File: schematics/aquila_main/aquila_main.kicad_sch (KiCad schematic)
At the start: 95 parts, among them IC1 TPS62152, IC2 TPS62132

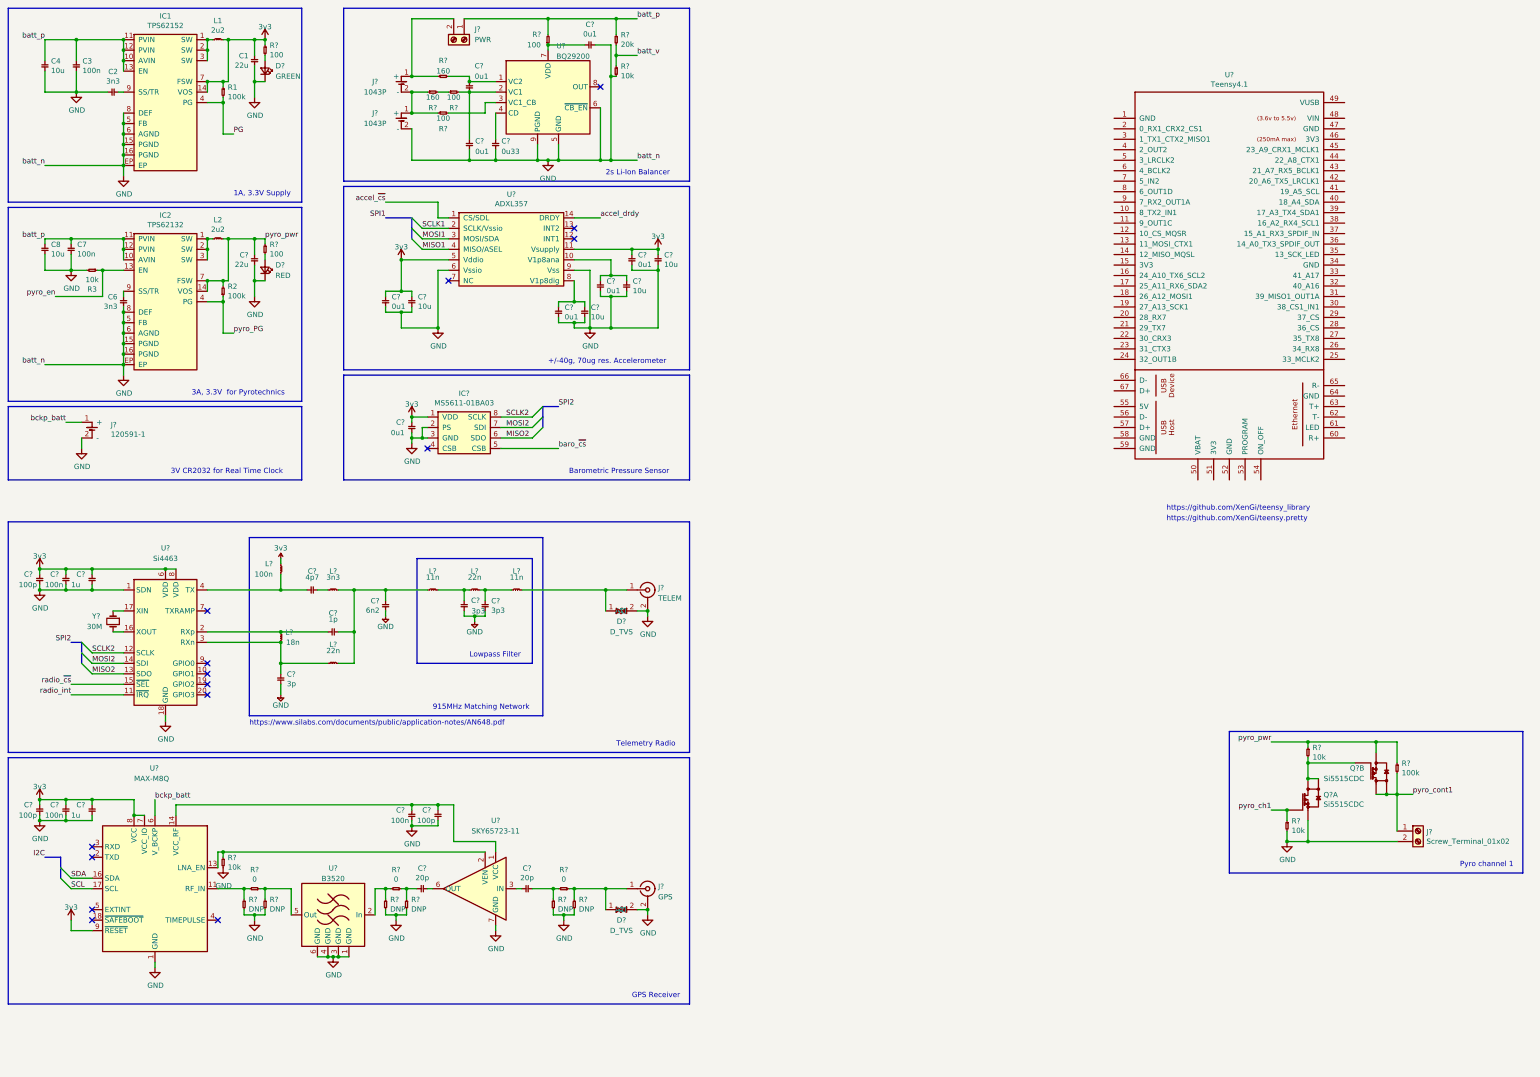
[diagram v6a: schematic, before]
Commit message: added connections for Teensy uC
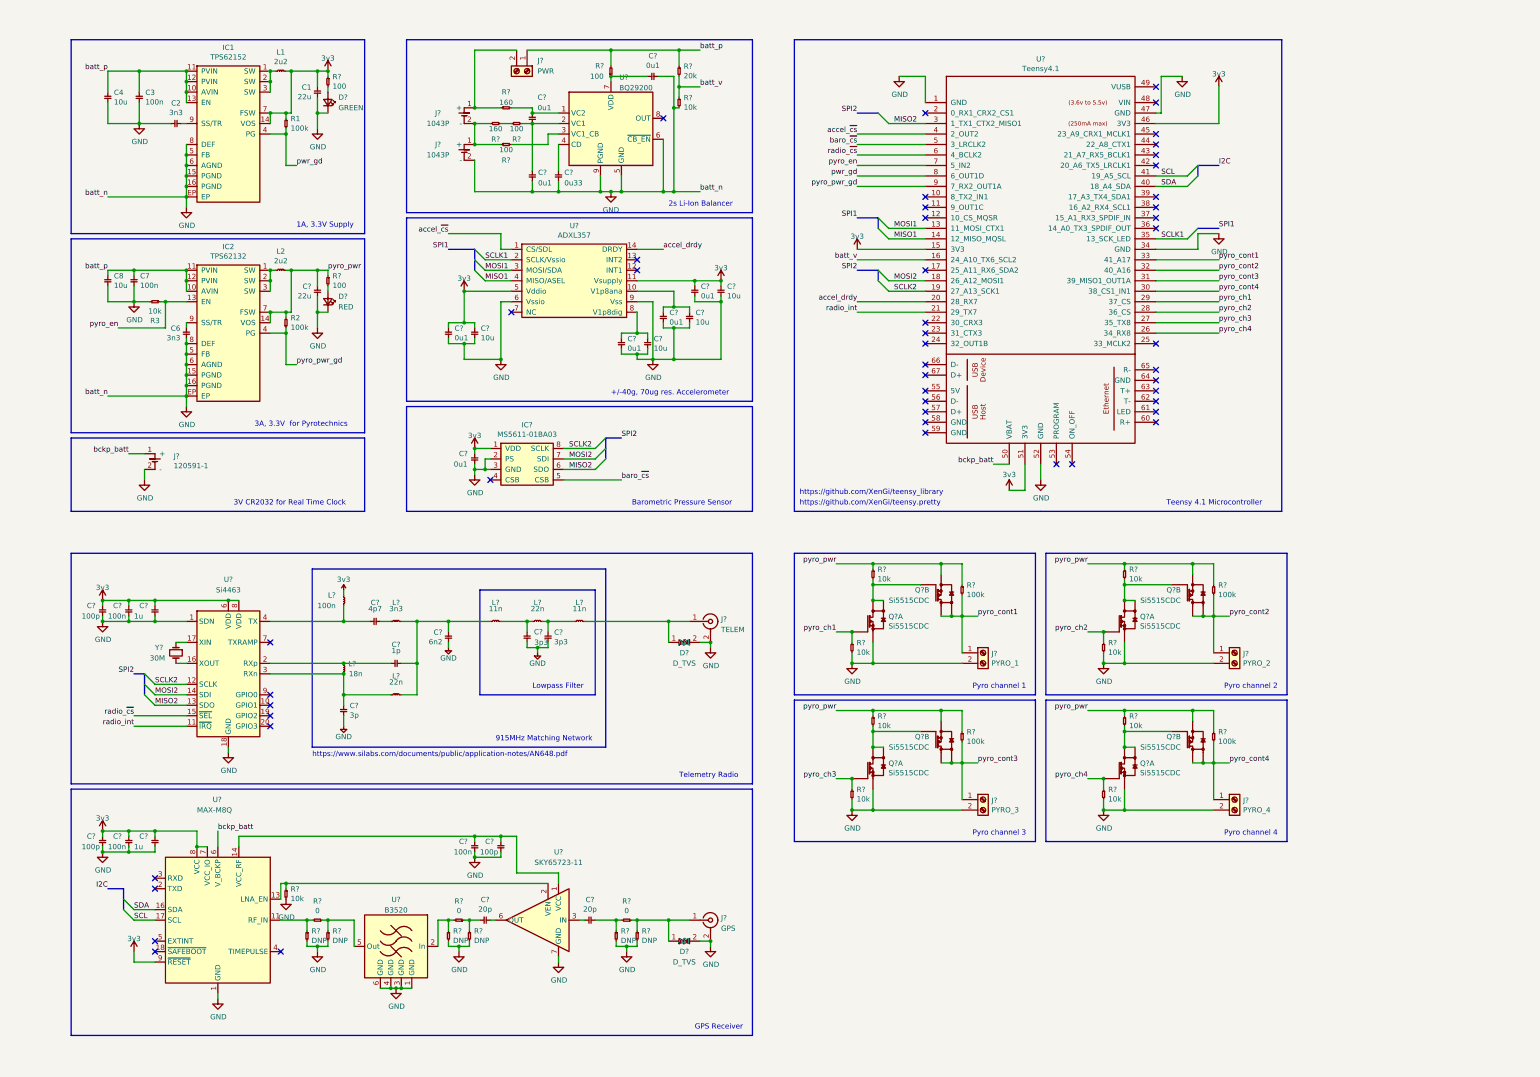
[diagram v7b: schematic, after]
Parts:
- added J?: PYRO_1, symbol Connector:Screw_Terminal_01x02
- added J?: PYRO_3, symbol Connector:Screw_Terminal_01x02
- added J?: PYRO_2, symbol Connector:Screw_Terminal_01x02
- added Q? (x6): Si5515CDC, cusf:ChipFET-1206-8, symbol aquila:Si5515CDC-cusf-kicad
- added R? (x3): 100k, symbol aquila:R-cusf-kicad
- added R? (x6): 10k, symbol aquila:R-cusf-kicad
- J?: value Screw_Terminal_01x02 -> PYRO_4
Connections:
- net PG is gone; now on net pwr_gd: IC1.4 (PG), R1.2
- net pyro_PG is gone; now on net pyro_pwr_gd: IC2.4 (PG), R2.1
- net +3V3: now also U?.15 (3V3), U?.46 (3V3), U?.51 (3V3)
- net GND: now also U?.1 (GND), U?.34 (GND), U?.47 (GND), U?.52 (GND), J?.2 (Pin_2), J?.2 (Pin_2), J?.2 (Pin_2), Q?.1 (S1), Q?.1 (S1), Q?.1 (S1), R?.2, R?.2, R?.2
- net MISO1: now also U?.14 (12_MISO_MQSL)
- net MISO2: now also U?.3 (1_TX1_CTX2_MISO1)
- net MOSI1: now also U?.13 (11_MOSI_CTX1)
- net MOSI2: now also U?.18 (26_A12_MOSI1)
- net SCL: now also U?.41 (19_A5_SCL)
- net SCLK1: now also U?.35 (13_SCK_LED)
- net SCLK2: now also U?.19 (27_A13_SCK1)
- net SDA: now also U?.40 (18_A4_SDA)
- net accel_drdy: now also U?.20 (28_RX7)
- net accel_~{cs}: now also U?.4 (2_OUT2)
- net baro_~{cs}: now also U?.5 (3_LRCLK2)
- net batt_v: now also U?.16 (24_A10_TX6_SCL2)
- net bckp_batt: now also U?.50 (VBAT)
- net pyro_ch1: now also U?.29 (37_CS), Q?.2 (G1), R?.1; no longer Q?.2 (G1), R?.1
- net pyro_cont1: now also U?.33 (41_A17), J?.1 (Pin_1), Q?.5 (D2), Q?.6 (D2), R?.2; no longer J?.1 (Pin_1), Q?.5 (D2), Q?.6 (D2), R?.2
- net pyro_en: now also U?.7 (5_IN2)
- net pyro_pwr: now also Q?.3 (S2), Q?.3 (S2), Q?.3 (S2), R?.1, R?.1, R?.1, R?.1, R?.1, R?.1
- net radio_int: now also U?.21 (29_TX7)
- net radio_~{cs}: now also U?.6 (4_BCLK2)
- net pyro_ch4: now reaches U?.26 (34_RX8)
- net pyro_ch4: now also Q?.2 (G1), R?.1
- net pyro_ch3: now reaches U?.27 (35_TX8)
- net pyro_ch3: now also Q?.2 (G1), R?.1
- net pyro_ch2: now reaches U?.28 (36_CS)
- net pyro_ch2: now also Q?.2 (G1), R?.1
- net pyro_cont4: now reaches U?.30 (38_CS1_IN1)
- net pyro_cont4: now also J?.1 (Pin_1), Q?.5 (D2), Q?.6 (D2), R?.2
- net pyro_cont3: now reaches U?.31 (39_MISO1_OUT1A)
- net pyro_cont3: now also J?.1 (Pin_1), Q?.5 (D2), Q?.6 (D2), R?.2
- net pyro_cont2: now reaches U?.32 (40_A16)
- net pyro_cont2: now also J?.1 (Pin_1), Q?.5 (D2), Q?.6 (D2), R?.2
- net pwr_gd: now reaches U?.8 (6_OUT1D)
- net pyro_pwr_gd: now reaches U?.9 (7_RX2_OUT1A)
- new net: Q?.4 (G2), Q?.7 (D1), Q?.8 (D1), R?.2 (x3)
- no-connect marks 15 -> 49
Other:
- note added: "Pyro channel 2"
- note added: "Pyro channel 3"
- note added: "Pyro channel 4"
- note added: "Teensy 4.1 Microcontroller"
- moved on the sheet: C1, C2, C3, C4, C6, C7, C8, C?, D?, IC1, IC2, IC?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

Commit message: designed out unobtainable components
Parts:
- removed C1, C?: 22u, symbol aquila:C-cusf-kicad
- removed C2, C6: 3n3, symbol aquila:C-cusf-kicad
- removed C3, C7: 100n, symbol aquila:C-cusf-kicad
- removed C4, C8: 10u, symbol aquila:C-cusf-kicad
- removed D?: RED, symbol Device:LED_Small
- removed IC1: TPS62152, cusf:QFN-16-EP-TI, symbol aquila:TPS62132
- removed IC2: TPS62132, cusf:QFN-16-EP-TI, symbol aquila:TPS62132
- removed L1, L2: 2u2, symbol aquila:L-cusf-kicad
- removed R1, R2: 100k, symbol aquila:R-cusf-kicad
- removed R3: 10k, symbol aquila:R-cusf-kicad
- removed R?: 100, symbol aquila:R-cusf-kicad
- added C? (x2): 1000u, symbol aquila:C-cusf-kicad
- added C? (x2): 22u, symbol aquila:C-cusf-kicad
- added D?: RED, symbol Device:LED_Small
- added L?: 68u, symbol aquila:L-cusf-kicad
- added L?: 150u, symbol aquila:L-cusf-kicad
- added R?: 100, symbol aquila:R-cusf-kicad
- added U? (x2): LM2576S-3.3/NOPB, symbol aquila:LM2576S-3.3/NOPB
- Q? (x8): value Si5515CDC -> IRF7509PbF; footprint cusf:ChipFET-1206-8 -> aquila:IRF7509PbF; symbol aquila:Si5515CDC-cusf-kicad -> aquila:IRF7509PbF; Farnell 2335332 -> 1611421
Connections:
- net +3V3: now also C?.1, L?.2, U?.4 (FD_BCK)
- net GND: now also C?.2, C?.2, C?.2, C?.2, D?.1 (K), U?.3 (GND), U?.3 (GND), U?.5 (~{ON}/OFF)
- net batt_p: now also C?.1, C?.1, U?.1 (VIN), U?.1 (VIN)
- net pyro_en: now also U?.5 (~{ON}/OFF)
- net pyro_pwr: now also C?.1, L?.2, R?.1, U?.4 (FD_BCK)
- net pwr_gd: no longer names the net of U?.8 (6_OUT1D)
- net pyro_pwr_gd: no longer names the net of U?.9 (7_RX2_OUT1A)
- new net: D?.2 (A), R?.2
- new net: L?.1, U?.2 (OUTPUT) (x2)
- no-connect marks 49 -> 51
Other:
- note added: "3A, 3.3V Supply"
- note removed: "1A, 3.3V Supply"
- moved on the sheet: D?, R?
